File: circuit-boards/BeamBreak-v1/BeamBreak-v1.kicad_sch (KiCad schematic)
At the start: 17 parts, among them J1 Power, J2 SENSOR, J3 OUT, U3 FODM121A

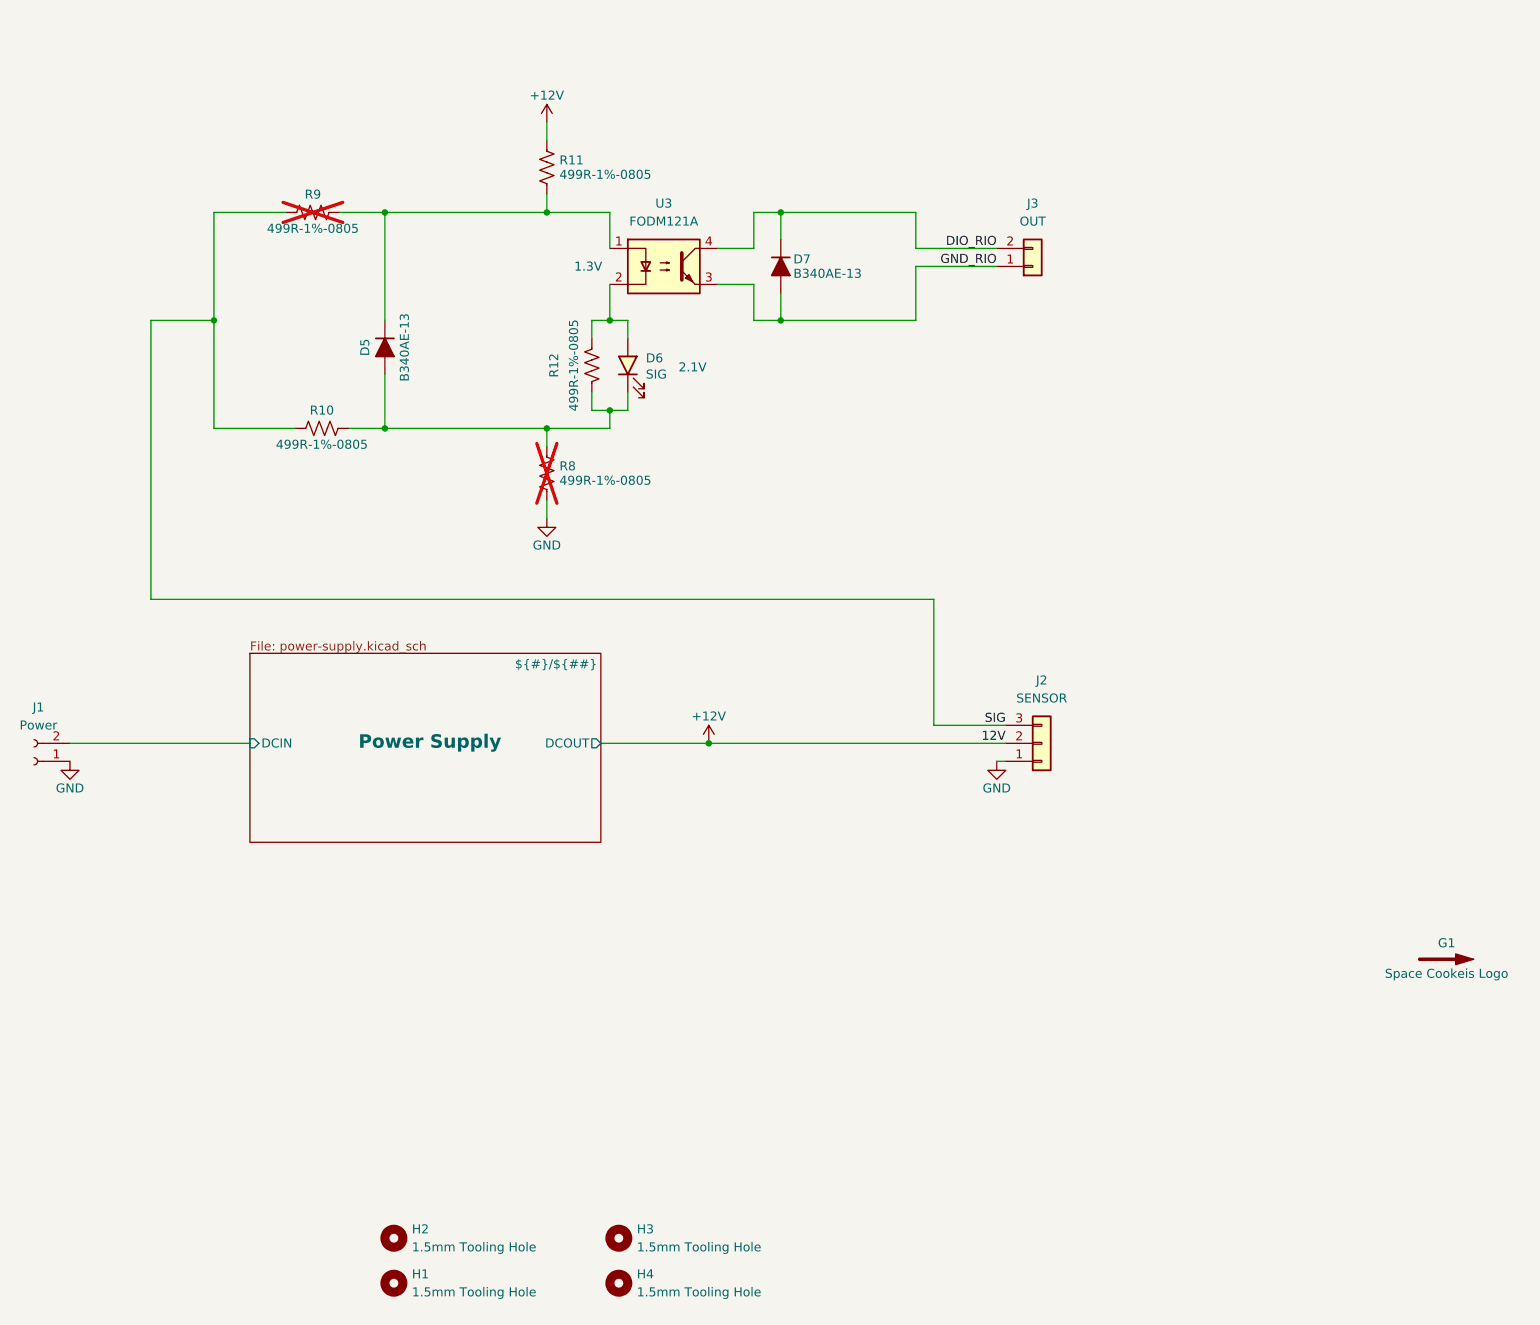
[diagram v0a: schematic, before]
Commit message: Chagned opto-coupler to totem pole output to drive 5V DIO with weak pull-up
Signed-off-by: Scott Berman <sgberman1@gmail.com>
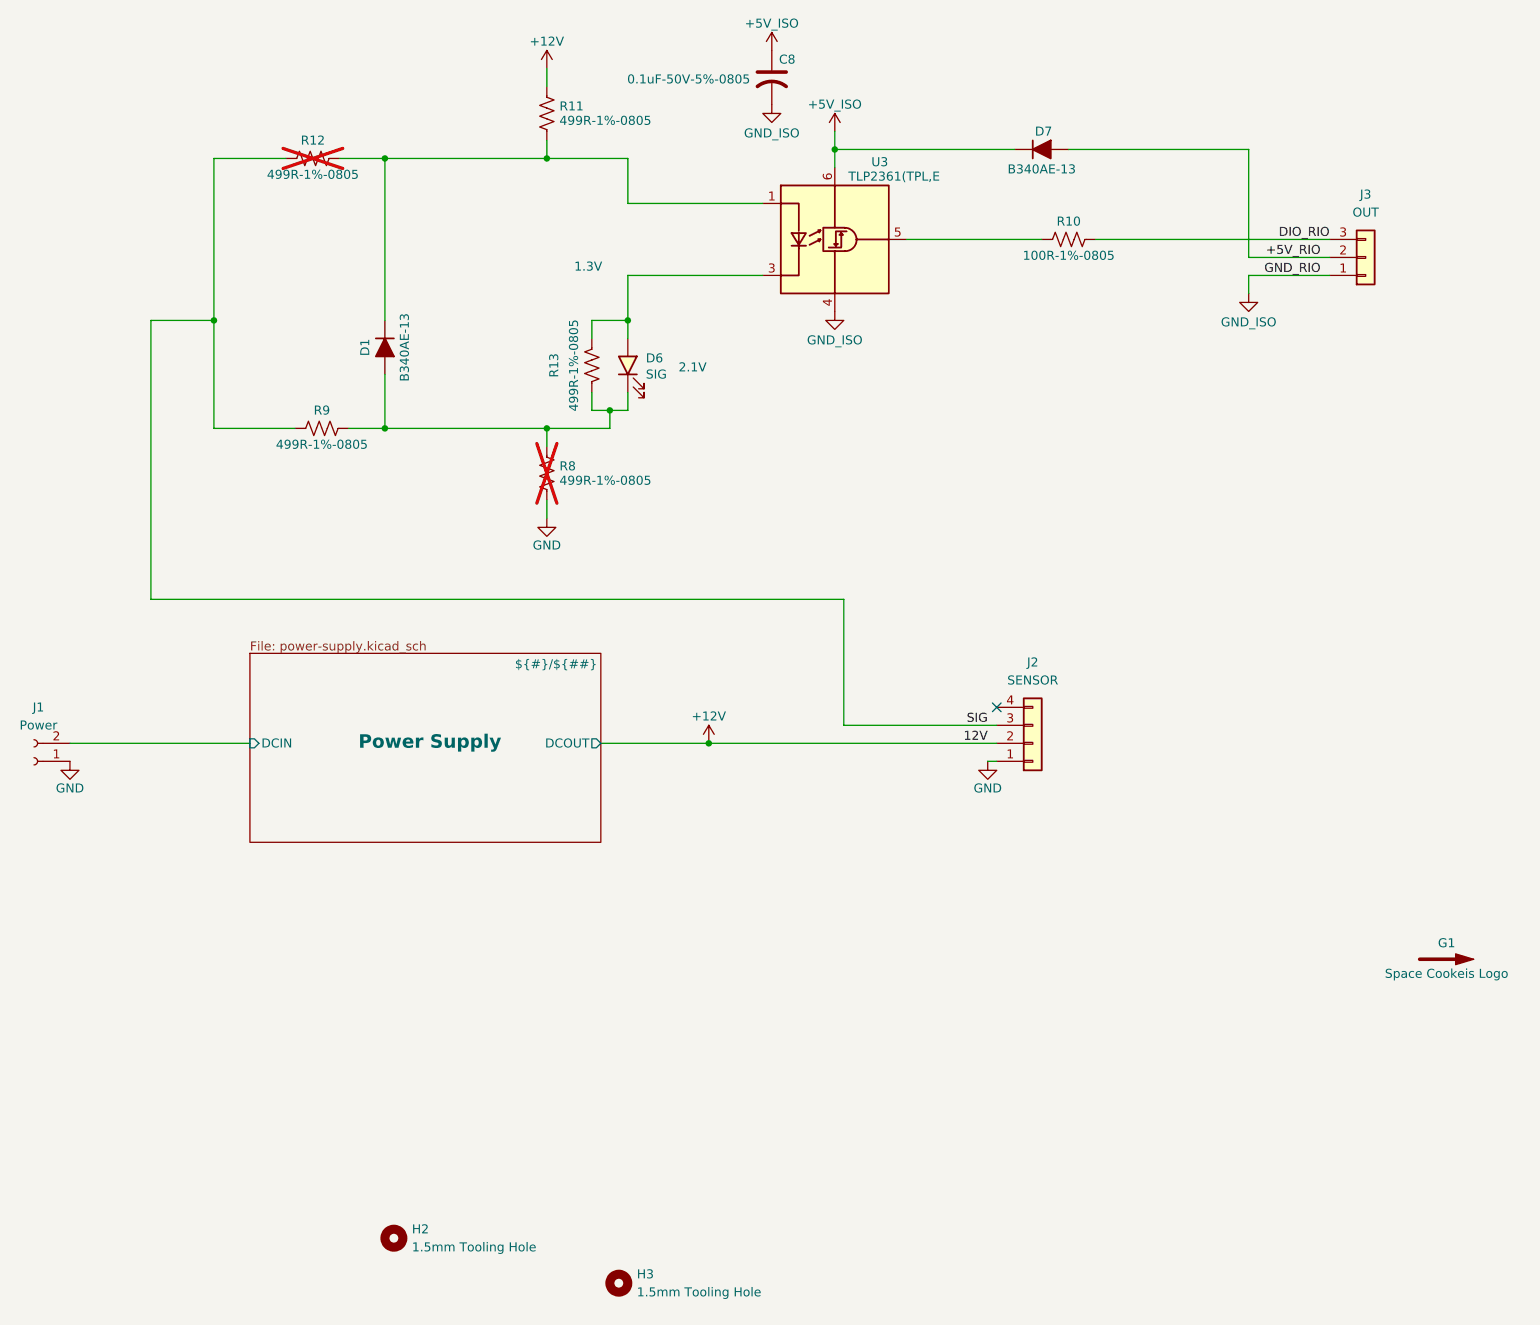
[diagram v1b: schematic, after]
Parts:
- removed H1, H3: 1.5mm Tooling Hole, BeamBreak:ToolingHole_1.5mm, symbol Mechanical:MountingHole
- removed J2: SENSOR, BeamBreak:Molex-70555-0002, symbol Connector_Generic:Conn_01x03
- removed J3: OUT, BeamBreak:Molex-70555-0001, symbol Connector_Generic:Conn_01x02
- removed U3: FODM121A, BeamBreak:onsemi-FODM121A, symbol Isolator:FODM217B
- added C8: 0.1uF-50V-5%-0805, Capacitor_SMD:C_0805_2012Metric_Pad1.18x1.45mm_HandSolder, symbol Device:C_US
- added J2: SENSOR, BeamBreak:Molex-70555-0003, symbol Connector_Generic:Conn_01x04
- added J3: OUT, BeamBreak:Molex-70555-0002, symbol Connector_Generic:Conn_01x03
- added R10: 100R-1%-0805, Resistor_SMD:R_0805_2012Metric_Pad1.20x1.40mm_HandSolder, symbol Device:R_US
- added U3: TLP2361(TPL,E, Package_SO:SO-5-6_4.55x3.7mm_P1.27mm, symbol Isolator:TLP2310
- renumbered D5 to D1, H4 to H3, R9 to R12, R12 to R13, R10 to R9
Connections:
- net +12V: now also J2.2 (Pin_2)
- net DIO_RIO: now also J3.3 (Pin_3), R10.2; no longer D7.1 (K)
- net GND: now also J2.1 (Pin_1)
- net SIG: now also J2.3 (Pin_3)
- net at D6.2 (A), R13.2: now also U3.3 (K)
- net at D1.1 (K), R11.1, R12.2: now also U3.1 (A)
- net GND_RIO renamed +5V_RIO
- net +5V_RIO: now also J3.2 (Pin_2)
- new net: R10.1, U3.5 (VO)
- new net +5V_ISO: C8.1, D7.1 (K), U3.6 (VDD)
- new net GND_ISO: C8.2, J3.1 (Pin_1), U3.4 (GND)
- no-connect marks 0 -> 1
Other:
- moved on the sheet: D7, R11, R12

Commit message: Improved placement and routing
Signed-off-by: Scott Berman <sgberman1@gmail.com>
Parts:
- added H1, H4: 1.5mm Tooling Hole, BeamBreak:ToolingHole_1.5mm, symbol Mechanical:MountingHole
- renumbered D6 to D5, D7 to D6, D1 to D7, R13 to R10, R10 to R11, R8 to R12, R12 to R13, R11 to R8
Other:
- moved on the sheet: H3
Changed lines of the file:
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@@
+	)
+	(symbol
+		(lib_id "Mechanical:MountingHole")
+		(at 201.93 248.92 0)
+		(unit 1)
+		(exclude_from_sim no)
+		(in_bom no)
+		(on_board yes)
+		(dnp no)
+		(fields_autoplaced yes)
+		(property "Reference" "H1"
+			(at 204.47 247.6499 0)
+			(effects
+				(font
+					(size 1.27 1.27)
+				)
+				(justify left)
+			)
+		)
+		(property "Value" "1.5mm Tooling Hole"
+			(at 204.47 250.1899 0)
+			(effects
+				(font
+					(size 1.27 1.27)
+				)
+				(justify left)
+			)
+		)
+		(property "Footprint" "BeamBreak:ToolingHole_1.5mm"
+			(at 201.93 248.92 0)
+			(effects
+				(font
+					(size 1.27 1.27)
+				)
+				(hide yes)
+			)
+		)
+		(property "Datasheet" "~"
+			(at 201.93 248.92 0)
+			(effects
+				(font
+					(size 1.27 1.27)
+				)
+				(hide yes)
+			)
+		)
+		(property "Description" ""
+			(at 201.93 248.92 0)
+			(effects
+				(font
+					(size 1.27 1.27)
+				)
+				(hide yes)
+			)
+		)
+		(instances
+			(project "BeamBreak-v1"
+				(path "/e06719a9-8757-4adc-9d1f-350085f61c1c"
+					(reference "H1")
+					(unit 1)
+				)
+			)
+		)
 	)
 	(symbol
@@
 		(on_board yes)
 		(dnp no)
-		(property "Reference" "R13"
+		(property "Reference" "R10"
 			(at 224.536 118.11 90)
 			(effects
@@
 			(project "BeamBreak-v1"
 				(path "/e06719a9-8757-4adc-9d1f-350085f61c1c"
-					(reference "R13")
+					(reference "R10")
 					(unit 1)
 				)
@@
 		(on_board yes)
 		(dnp no)
-		(property "Reference" "D1"
+		(property "Reference" "D7"
 			(at 197.866 115.57 0)
 			(effects
@@
 			(project "BeamBreak-v1"
 				(path "/e06719a9-8757-4adc-9d1f-350085f61c1c"
-					(reference "D1")
+					(reference "D7")
 					(unit 1)
 				)
@@
 		(on_board yes)
 		(dnp yes)
-		(property "Reference" "R8"
+		(property "Reference" "R12"
 			(at 225.298 132.334 0)
 			(effects
@@
 			(project "BeamBreak-v1"
 				(path "/e06719a9-8757-4adc-9d1f-350085f61c1c"
-					(reference "R8")
+					(reference "R12")
 					(unit 1)
 				)
@@
 	)
 	(symbol
+		(lib_id "Mechanical:MountingHole")
+		(at 233.68 241.3 0)
+		(unit 1)
+		(exclude_from_sim no)
+		(in_bom no)
+		(on_board yes)
+		(dnp no)
+		(fields_autoplaced yes)
+		(property "Reference" "H4"
+			(at 236.22 240.0299 0)
+			(effects
+				(font
+					(size 1.27 1.27)
+				)
+				(justify left)
+			)
+		)
+		(property "Value" "1.5mm Tooling Hole"
+			(at 236.22 242.5699 0)
+			(effects
+				(font
+					(size 1.27 1.27)
+				)
+				(justify left)
+			)
+		)
+		(property "Footprint" "BeamBreak:ToolingHole_1.5mm"
+			(at 233.68 241.3 0)
+			(effects
+				(font
+					(size 1.27 1.27)
+				)
+				(hide yes)
+			)
+		)
+		(property "Datasheet" "~"
+			(at 233.68 241.3 0)
+			(effects
+				(font
+					(size 1.27 1.27)
+				)
+				(hide yes)
+			)
+		)
+		(property "Description" ""
+			(at 233.68 241.3 0)
+			(effects
+				(font
+					(size 1.27 1.27)
+				)
+				(hide yes)
+			)
+		)
+		(instances
+			(project "BeamBreak-v1"
+				(path "/e06719a9-8757-4adc-9d1f-350085f61c1c"
+					(reference "H4")
+					(unit 1)
+				)
+			)
+		)
+	)
+	(symbol
 		(lib_id "power:GND")
 		(at 156.21 173.99 0)
@@
 		(on_board yes)
 		(dnp no)
-		(property "Reference" "D6"
+		(property "Reference" "D5"
 			(at 237.49 117.094 90)
 			(effects
@@
 			(project "BeamBreak-v1"
 				(path "/e06719a9-8757-4adc-9d1f-350085f61c1c"
-					(reference "D6")
+					(reference "D5")
 					(unit 1)
 				)
@@
 		(on_board yes)
 		(dnp no)
-		(property "Reference" "R11"
+		(property "Reference" "R8"
 			(at 225.298 81.534 0)
 			(effects
@@
 			(project "BeamBreak-v1"
 				(path "/e06719a9-8757-4adc-9d1f-350085f61c1c"
-					(reference "R11")
+					(reference "R8")
 					(unit 1)
 				)
@@
 		(on_board yes)
 		(dnp no)
-		(property "Reference" "D7"
+		(property "Reference" "D6"
 			(at 293.624 85.09 0)
 			(effects
@@
 			(project "BeamBreak-v1"
 				(path "/e06719a9-8757-4adc-9d1f-350085f61c1c"
-					(reference "D7")
+					(reference "D6")
 					(unit 1)
 				)
@@
 	(symbol
 		(lib_id "Mechanical:MountingHole")
-		(at 233.68 247.65 0)
+		(at 233.68 248.92 0)
 		(unit 1)
 		(exclude_from_sim no)
@@
 		(fields_autoplaced yes)
 		(property "Reference" "H3"
-			(at 236.22 246.3799 0)
+			(at 236.22 247.6499 0)
 			(effects
 				(font
@@
 		)
 		(property "Value" "1.5mm Tooling Hole"
-			(at 236.22 248.9199 0)
+			(at 236.22 250.1899 0)
 			(effects
 				(font
@@
 		)
 		(property "Footprint" "BeamBreak:ToolingHole_1.5mm"
-			(at 233.68 247.65 0)
+			(at 233.68 248.92 0)
 			(effects
 				(font
@@
 		)
 		(property "Datasheet" "~"
-			(at 233.68 247.65 0)
+			(at 233.68 248.92 0)
 			(effects
 				(font
@@
 		)
 		(property "Description" ""
-			(at 233.68 247.65 0)
+			(at 233.68 248.92 0)
 			(effects
 				(font
@@
 		(on_board yes)
 		(dnp yes)
-		(property "Reference" "R12"
+		(property "Reference" "R13"
 			(at 190.5 86.36 90)
 			(effects
@@
 			(project "BeamBreak-v1"
 				(path "/e06719a9-8757-4adc-9d1f-350085f61c1c"
-					(reference "R12")
+					(reference "R13")
 					(unit 1)
 				)
@@
 		(on_board yes)
 		(dnp no)
-		(property "Reference" "R10"
+		(property "Reference" "R11"
 			(at 297.18 97.79 90)
 			(effects
@@
 			(project "BeamBreak-v1"
 				(path "/e06719a9-8757-4adc-9d1f-350085f61c1c"
-					(reference "R10")
-					(unit 1)
-				)
+					(reference "R11")
+					(unit 1)
+				)

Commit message: Changed Signal LED to Yellow
Signed-off-by: Scott Berman <sgberman1@gmail.com>
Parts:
- D5: DIST P/N 1080-1419-1-ND -> 1080-1418-1-ND; MFG P/N QTLP650D4TR/QT15-21SYGD/S530-E2/TR8 -> QTLP650D3TR
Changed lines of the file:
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@@
 			)
 		)
-		(property "DIST P/N" "1080-1419-1-ND"
+		(property "DIST P/N" "1080-1418-1-ND"
 			(at 234.95 118.11 0)
 			(effects
@@
 			)
 		)
-		(property "MFG P/N" "QTLP650D4TR/QT15-21SYGD/S530-E2/TR8"
+		(property "MFG P/N" "QTLP650D3TR"
 			(at 234.95 118.11 0)
 			(effects
